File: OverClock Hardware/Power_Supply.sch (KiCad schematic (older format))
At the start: 10 parts

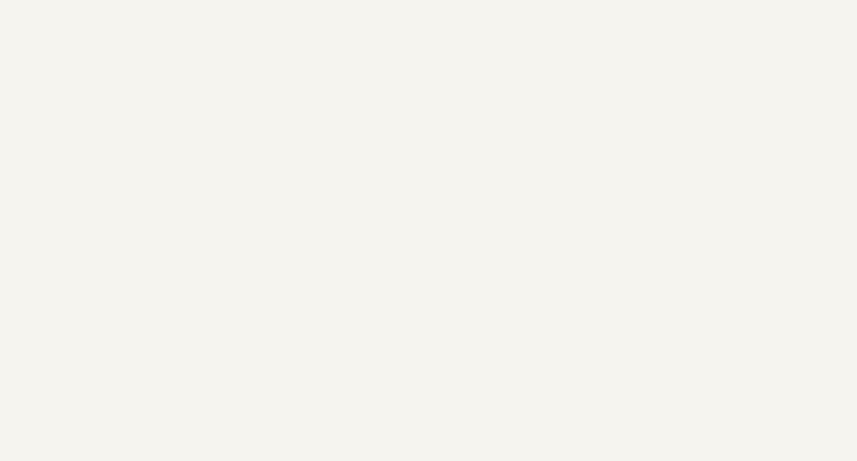
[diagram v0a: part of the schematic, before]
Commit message: Added JTAG Header
Added a JTAG header and interfaced it to the FPGA as per: page 16 https://www.intel.com/content/dam/www/programmable/us/en/pdfs/literature/hb/max-10/m10_guidelines.pdf
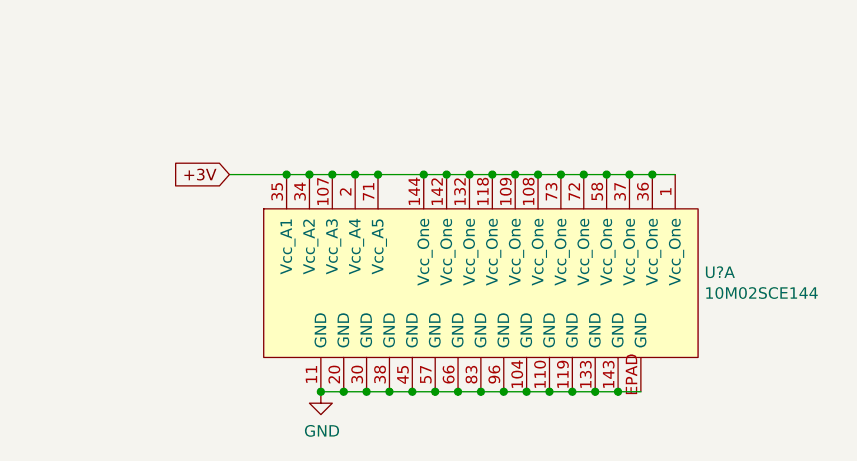
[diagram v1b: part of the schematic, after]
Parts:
- added U?: 10M02SCE144, Maxted Libs:QFP-144_EPAD_20x20_Pitch0.5mm, symbol Maxted_Libs:10M02SCE144
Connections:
- wire segments 41 -> 72
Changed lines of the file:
@@
 	7150 1400 7000 1400
 Connection ~ 7000 1400
+$Comp
+L Maxted_Libs:10M02SCE144 U?
+U 1 1 5C66E890
+P 6950 3900
+F 0 "U?" H 7928 4021 50  0000 L CNN
+F 1 "10M02SCE144" H 7928 3930 50  0000 L CNN
+F 2 "Maxted Libs:QFP-144_EPAD_20x20_Pitch0.5mm" H 7950 4700 50  0001 C CNN
+F 3 "" V 7300 4050 50  0001 C CNN
+	1    6950 3900
+	1    0    0    -1
+$EndComp
+$Comp
+L power:GND #PWR?
+U 1 1 5C66E982
+P 6250 4300
+F 0 "#PWR?" H 6250 4050 50  0001 C CNN
+F 1 "GND" H 6255 4127 50  0000 C CNN
+F 2 "" H 6250 4300 50  0001 C CNN
+F 3 "" H 6250 4300 50  0001 C CNN
+	1    6250 4300
+	1    0    0    -1
+$EndComp
+Wire Wire Line
+	7650 4300 7550 4300
+Connection ~ 6250 4300
+Connection ~ 6350 4300
+Wire Wire Line
+	6350 4300 6250 4300
+Connection ~ 6450 4300
+Wire Wire Line
+	6450 4300 6350 4300
+Connection ~ 6550 4300
+Wire Wire Line
+	6550 4300 6450 4300
+Connection ~ 6650 4300
+Wire Wire Line
+	6650 4300 6550 4300
+Connection ~ 6750 4300
+Wire Wire Line
+	6750 4300 6650 4300
+Connection ~ 6850 4300
+Wire Wire Line
+	6850 4300 6750 4300
+Connection ~ 6950 4300
+Wire Wire Line
+	6950 4300 6850 4300
+Connection ~ 7050 4300
+Wire Wire Line
+	7050 4300 6950 4300
+Connection ~ 7150 4300
+Wire Wire Line
+	7150 4300 7050 4300
+Connection ~ 7250 4300
+Wire Wire Line
+	7250 4300 7150 4300
+Connection ~ 7350 4300
+Wire Wire Line
+	7350 4300 7250 4300
+Connection ~ 7450 4300
+Wire Wire Line
+	7450 4300 7350 4300
+Connection ~ 7550 4300
+Wire Wire Line
+	7550 4300 7450 4300
+Wire Wire Line
+	7800 3350 7700 3350
+Connection ~ 6200 3350
+Wire Wire Line
+	6200 3350 6100 3350
+Connection ~ 6300 3350
+Wire Wire Line
+	6300 3350 6200 3350
+Connection ~ 6400 3350
+Wire Wire Line
+	6400 3350 6300 3350
+Connection ~ 6500 3350
+Wire Wire Line
+	6500 3350 6400 3350
+Connection ~ 6700 3350
+Wire Wire Line
+	6700 3350 6500 3350
+Connection ~ 6800 3350
+Wire Wire Line
+	6800 3350 6700 3350
+Connection ~ 6900 3350
+Wire Wire Line
+	6900 3350 6800 3350
+Connection ~ 7000 3350
+Wire Wire Line
+	7000 3350 6900 3350
+Connection ~ 7100 3350
+Wire Wire Line
+	7100 3350 7000 3350
+Connection ~ 7200 3350
+Wire Wire Line
+	7200 3350 7100 3350
+Connection ~ 7300 3350
+Wire Wire Line
+	7300 3350 7200 3350
+Connection ~ 7400 3350
+Wire Wire Line
+	7400 3350 7300 3350
+Connection ~ 7500 3350
+Wire Wire Line
+	7500 3350 7400 3350
+Connection ~ 7600 3350
+Wire Wire Line
+	7600 3350 7500 3350
+Connection ~ 7700 3350
+Wire Wire Line
+	7700 3350 7600 3350
+Text GLabel 5850 3350 0    50   Input ~ 0
++3V
+Wire Wire Line
+	5850 3350 6100 3350
+Connection ~ 6100 3350
 $EndSCHEMATC

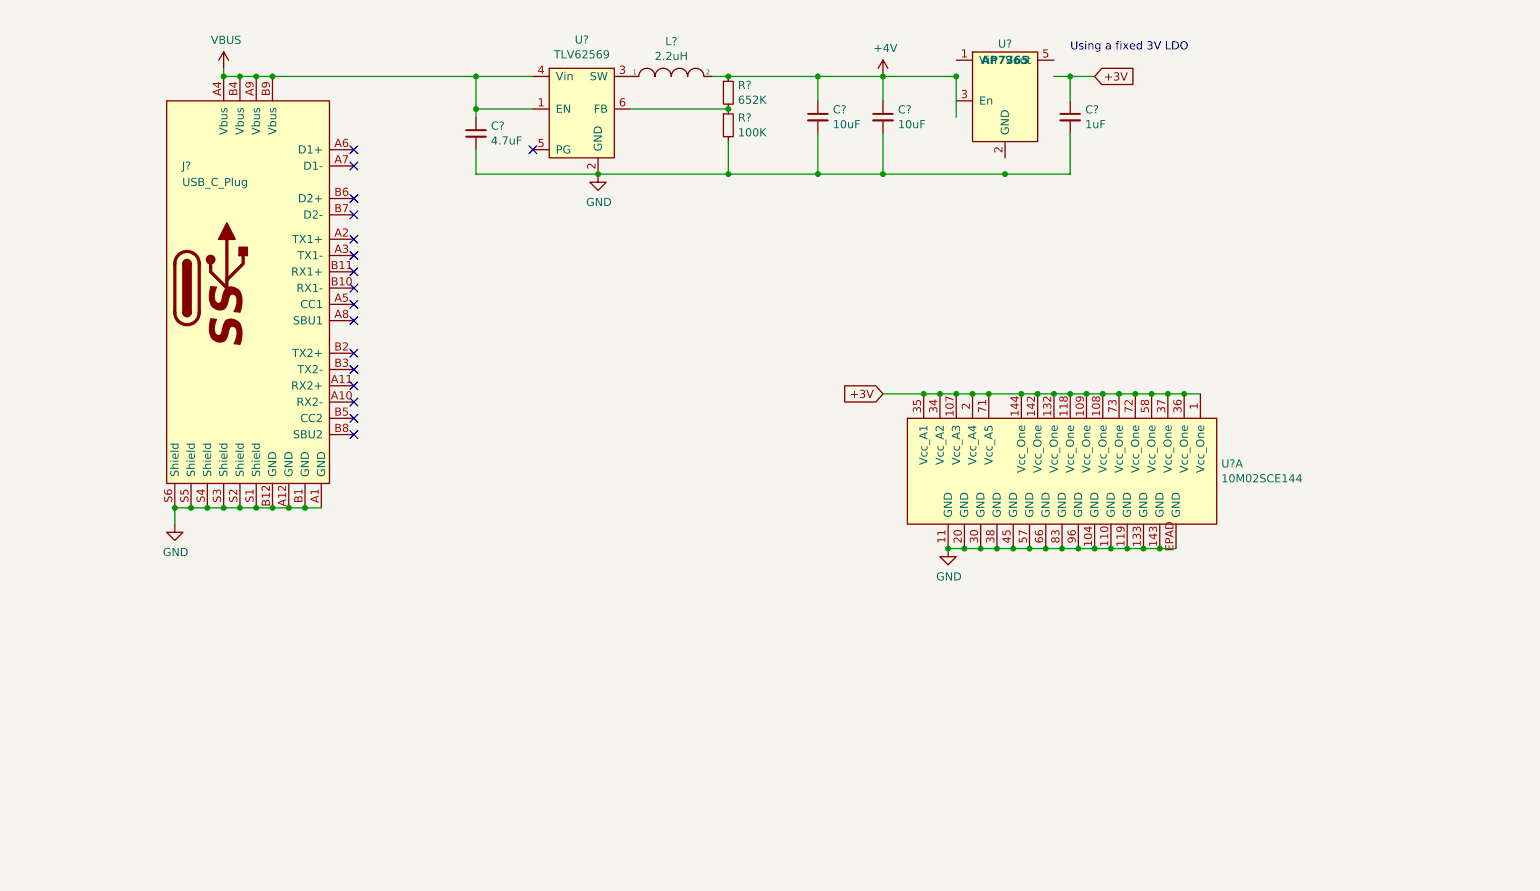
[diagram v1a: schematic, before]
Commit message: Added Decoupling strategy and started adding decoupling capacitors
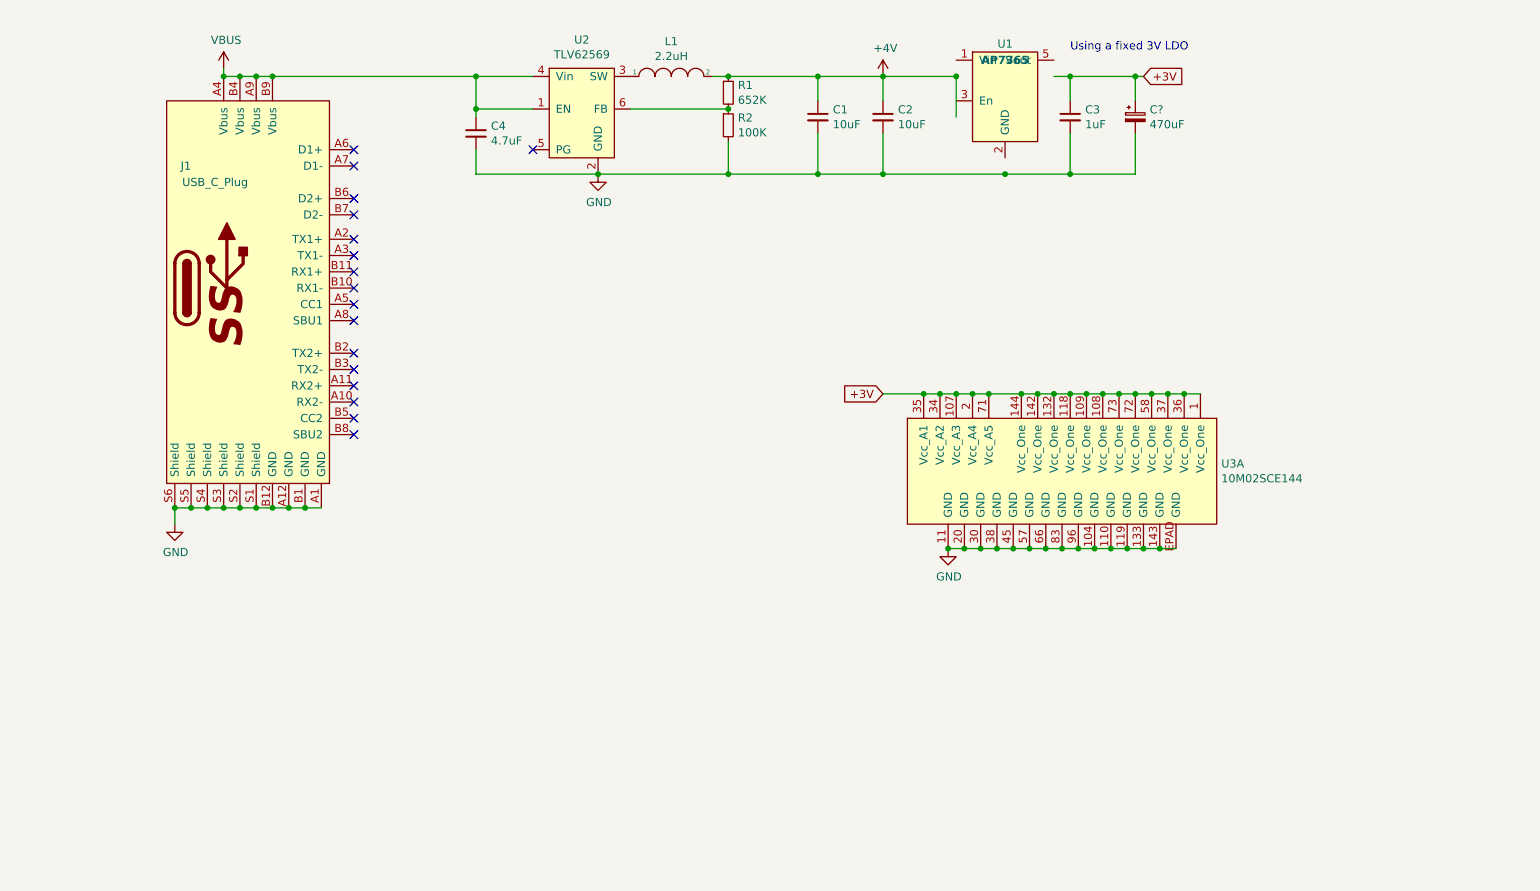
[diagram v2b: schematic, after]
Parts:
- added C?: 470uF, symbol Device:CP_Small
- gave numbers to parts that had none: 11
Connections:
- wire segments 72 -> 76
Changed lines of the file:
@@
 P 1950 2700
 AR Path="/5C666559" Ref="J?"  Part="1"
-AR Path="/5C656C49/5C666559" Ref="J?"  Part="1"
-F 0 "J?" H 1600 3450 50  0000 R CNN
+AR Path="/5C656C49/5C666559" Ref="J1"  Part="1"
+F 0 "J1" H 1600 3450 50  0000 R CNN
 F 1 "USB_C_Plug" H 1950 3350 50  0000 R CNN
 F 2 "Maxted Libs:Hirose_USB_C_Connector" H 2600 3050 50  0001 C CNN
@@
 P 1500 4150
 AR Path="/5C666560" Ref="#PWR?"  Part="1"
-AR Path="/5C656C49/5C666560" Ref="#PWR?"  Part="1"
-F 0 "#PWR?" H 1500 3900 50  0001 C CNN
+AR Path="/5C656C49/5C666560" Ref="#PWR04"  Part="1"
+F 0 "#PWR04" H 1500 3900 50  0001 C CNN
 F 1 "GND" H 1505 3977 50  0000 C CNN
 F 2 "" H 1500 4150 50  0001 C CNN
@@
 P 1800 1350
 AR Path="/5C666579" Ref="#PWR?"  Part="1"
-AR Path="/5C656C49/5C666579" Ref="#PWR?"  Part="1"
-F 0 "#PWR?" H 1800 1200 50  0001 C CNN
+AR Path="/5C656C49/5C666579" Ref="#PWR01"  Part="1"
+F 0 "#PWR01" H 1800 1200 50  0001 C CNN
 F 1 "VBUS" H 1815 1523 50  0000 C CNN
 F 2 "" H 1800 1350 50  0001 C CNN
@@
 P 3950 1650
 AR Path="/5C666597" Ref="U?"  Part="1"
-AR Path="/5C656C49/5C666597" Ref="U?"  Part="1"
-F 0 "U?" H 4000 2125 50  0000 C CNN
+AR Path="/5C656C49/5C666597" Ref="U2"  Part="1"
+F 0 "U2" H 4000 2125 50  0000 C CNN
 F 1 "TLV62569" H 4000 2034 50  0000 C CNN
 F 2 "Maxted Libs:SOT23-6" H 3600 1350 50  0001 C CNN
@@
 P 4100 2000
 AR Path="/5C6665A0" Ref="#PWR?"  Part="1"
-AR Path="/5C656C49/5C6665A0" Ref="#PWR?"  Part="1"
-F 0 "#PWR?" H 4100 1750 50  0001 C CNN
+AR Path="/5C656C49/5C6665A0" Ref="#PWR03"  Part="1"
+F 0 "#PWR03" H 4100 1750 50  0001 C CNN
 F 1 "GND" H 4105 1827 50  0000 C CNN
 F 2 "" H 4100 2000 50  0001 C CNN
@@
 P 4550 1400
 AR Path="/5C6665A7" Ref="L?"  Part="1"
-AR Path="/5C656C49/5C6665A7" Ref="L?"  Part="1"
-F 0 "L?" H 4550 1615 50  0000 C CNN
+AR Path="/5C656C49/5C6665A7" Ref="L1"  Part="1"
+F 0 "L1" H 4550 1615 50  0000 C CNN
 F 1 "2.2uH" H 4550 1524 50  0000 C CNN
 F 2 "Maxted Libs:IHLP3232" H 4550 1400 50  0001 C CNN
@@
 P 4900 1500
 AR Path="/5C6665AE" Ref="R?"  Part="1"
-AR Path="/5C656C49/5C6665AE" Ref="R?"  Part="1"
-F 0 "R?" H 4959 1546 50  0000 L CNN
+AR Path="/5C656C49/5C6665AE" Ref="R1"  Part="1"
+F 0 "R1" H 4959 1546 50  0000 L CNN
 F 1 "652K" H 4959 1455 50  0000 L CNN
 F 2 "Resistor_SMD:R_0805_2012Metric_Pad1.15x1.40mm_HandSolder" H 4900 1500 50  0001 C CNN
@@
 P 4900 1700
 AR Path="/5C6665B5" Ref="R?"  Part="1"
-AR Path="/5C656C49/5C6665B5" Ref="R?"  Part="1"
-F 0 "R?" H 4959 1746 50  0000 L CNN
+AR Path="/5C656C49/5C6665B5" Ref="R2"  Part="1"
+F 0 "R2" H 4959 1746 50  0000 L CNN
 F 1 "100K" H 4959 1655 50  0000 L CNN
 F 2 "Resistor_SMD:R_0805_2012Metric_Pad1.15x1.40mm_HandSolder" H 4900 1700 50  0001 C CNN
@@
 P 5450 1650
 AR Path="/5C6665BF" Ref="C?"  Part="1"
-AR Path="/5C656C49/5C6665BF" Ref="C?"  Part="1"
-F 0 "C?" H 5542 1696 50  0000 L CNN
+AR Path="/5C656C49/5C6665BF" Ref="C1"  Part="1"
+F 0 "C1" H 5542 1696 50  0000 L CNN
 F 1 "10uF" H 5542 1605 50  0000 L CNN
 F 2 "Capacitor_SMD:C_0805_2012Metric_Pad1.15x1.40mm_HandSolder" H 5450 1650 50  0001 C CNN
@@
 P 5850 1650
 AR Path="/5C6665C6" Ref="C?"  Part="1"
-AR Path="/5C656C49/5C6665C6" Ref="C?"  Part="1"
-F 0 "C?" H 5942 1696 50  0000 L CNN
+AR Path="/5C656C49/5C6665C6" Ref="C2"  Part="1"
+F 0 "C2" H 5942 1696 50  0000 L CNN
 F 1 "10uF" H 5942 1605 50  0000 L CNN
 F 2 "Capacitor_SMD:C_0805_2012Metric_Pad1.15x1.40mm_HandSolder" H 5850 1650 50  0001 C CNN
@@
 P 3350 1750
 AR Path="/5C6665DC" Ref="C?"  Part="1"
-AR Path="/5C656C49/5C6665DC" Ref="C?"  Part="1"
-F 0 "C?" H 3442 1796 50  0000 L CNN
+AR Path="/5C656C49/5C6665DC" Ref="C4"  Part="1"
+F 0 "C4" H 3442 1796 50  0000 L CNN
 F 1 "4.7uF" H 3442 1705 50  0000 L CNN
 F 2 "Capacitor_SMD:C_0805_2012Metric_Pad1.15x1.40mm_HandSolder" H 3350 1750 50  0001 C CNN
@@
 P 5850 1400
 AR Path="/5C6665EC" Ref="#PWR?"  Part="1"
-AR Path="/5C656C49/5C6665EC" Ref="#PWR?"  Part="1"
-F 0 "#PWR?" H 5850 1250 50  0001 C CNN
+AR Path="/5C656C49/5C6665EC" Ref="#PWR02"  Part="1"
+F 0 "#PWR02" H 5850 1250 50  0001 C CNN
 F 1 "+4V" H 5865 1573 50  0000 C CNN
 F 2 "" H 5850 1400 50  0001 C CNN
@@
 P 6600 1500
 AR Path="/5C6665F4" Ref="U?"  Part="1"
-AR Path="/5C656C49/5C6665F4" Ref="U?"  Part="1"
-F 0 "U?" H 6600 1800 50  0000 C CNN
+AR Path="/5C656C49/5C6665F4" Ref="U1"  Part="1"
+F 0 "U1" H 6600 1800 50  0000 C CNN
 F 1 "AP7365" H 6600 1700 50  0000 C CNB
 F 2 "Maxted Libs:SOT-23-5" H 6600 950 50  0001 C CNN
@@
 	5850 2000 6600 2000
 Connection ~ 5850 2000
-Text GLabel 7150 1400 2    50   Input ~ 0
+Text GLabel 7450 1400 2    50   Input ~ 0
 +3V
 $Comp
@@
 P 7000 1650
 AR Path="/5C666601" Ref="C?"  Part="1"
-AR Path="/5C656C49/5C666601" Ref="C?"  Part="1"
-F 0 "C?" H 7092 1696 50  0000 L CNN
+AR Path="/5C656C49/5C666601" Ref="C3"  Part="1"
+F 0 "C3" H 7092 1696 50  0000 L CNN
 F 1 "1uF" H 7092 1605 50  0000 L CNN
 F 2 "Capacitor_SMD:C_0805_2012Metric_Pad1.15x1.40mm_HandSolder" H 7000 1650 50  0001 C CNN
@@
 Wire Wire Line
 	7000 1750 7000 2000
-Wire Wire Line
-	7150 1400 7000 1400
 Connection ~ 7000 1400
 $Comp
-L Maxted_Libs:10M02SCE144 U?
+L Maxted_Libs:10M02SCE144 U3
 U 1 1 5C66E890
 P 6950 3900
-F 0 "U?" H 7928 4021 50  0000 L CNN
+F 0 "U3" H 7928 4021 50  0000 L CNN
 F 1 "10M02SCE144" H 7928 3930 50  0000 L CNN
 F 2 "Maxted Libs:QFP-144_EPAD_20x20_Pitch0.5mm" H 7950 4700 50  0001 C CNN
@@
 $EndComp
 $Comp
-L power:GND #PWR?
+L power:GND #PWR05
 U 1 1 5C66E982
 P 6250 4300
-F 0 "#PWR?" H 6250 4050 50  0001 C CNN
+F 0 "#PWR05" H 6250 4050 50  0001 C CNN
 F 1 "GND" H 6255 4127 50  0000 C CNN
 F 2 "" H 6250 4300 50  0001 C CNN
@@
 	5850 3350 6100 3350
 Connection ~ 6100 3350
+Wire Wire Line
+	7000 1400 7400 1400
+Wire Wire Line
+	7400 1550 7400 1400
+Connection ~ 7400 1400
+Wire Wire Line
+	7400 1400 7450 1400
+Wire Wire Line
+	7400 1750 7400 2000
+Wire Wire Line
+	7400 2000 7000 2000
+Connection ~ 7000 2000
+$Comp
+L Device:CP_Small C?
+U 1 1 5C6DC80E
+P 7400 1650
+F 0 "C?" H 7488 1696 50  0000 L CNN
+F 1 "470uF" H 7488 1605 50  0000 L CNN
+F 2 "" H 7400 1650 50  0001 C CNN
+F 3 "~" H 7400 1650 50  0001 C CNN
+	1    7400 1650
+	1    0    0    -1
+$EndComp
 $EndSCHEMATC

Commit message: Added Decoupling Caps for FPGA core
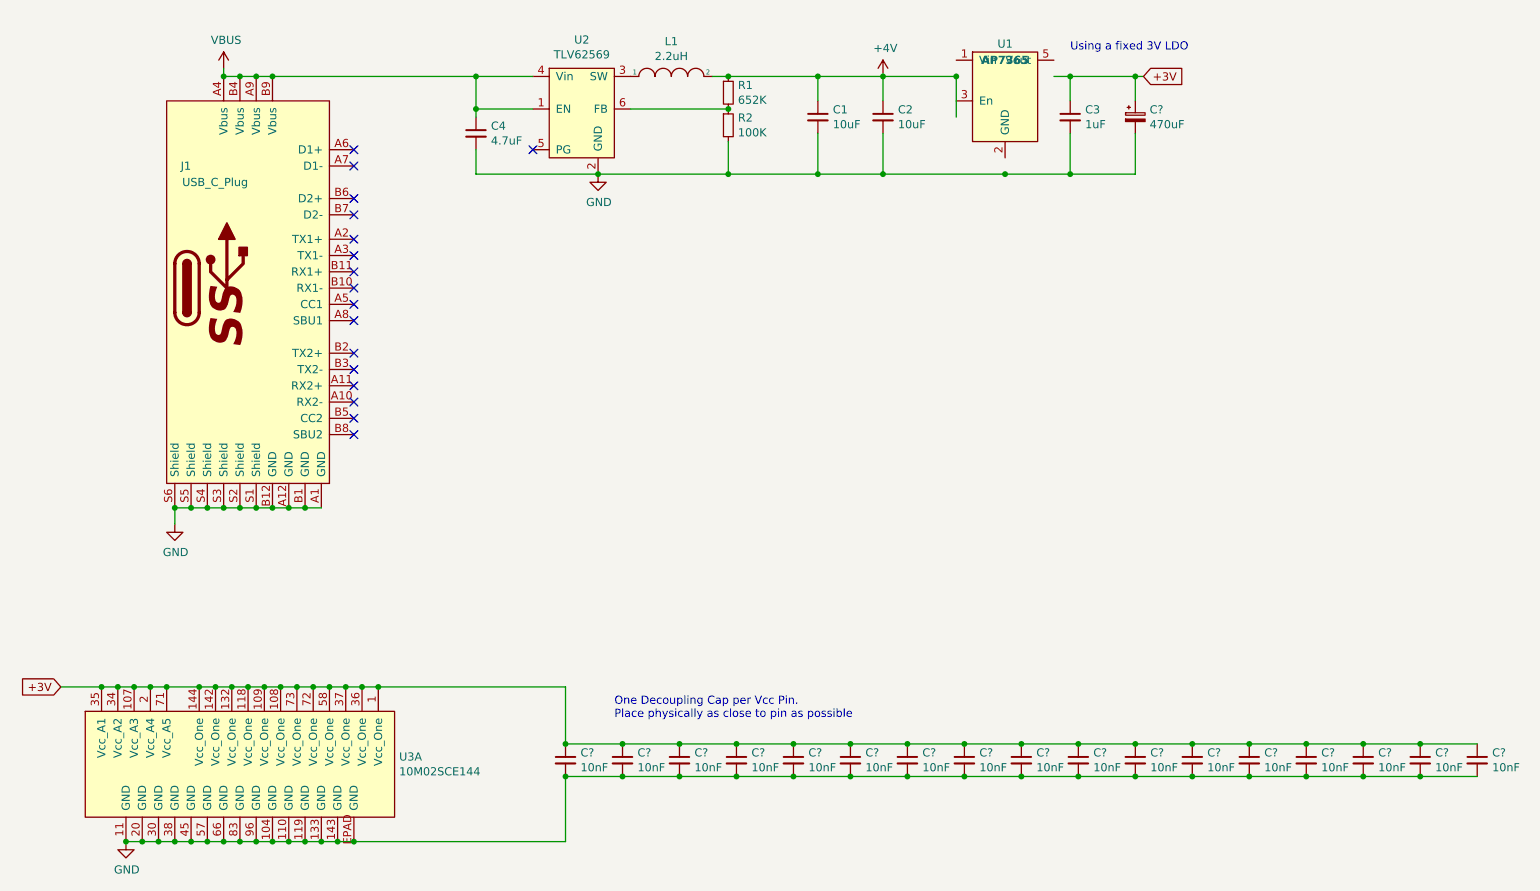
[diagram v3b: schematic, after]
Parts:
- added C? (x17): 10nF, Capacitor_SMD:C_0603_1608Metric_Pad1.05x0.95mm_HandSolder, symbol Device:C_Small
- C?: footprint (none) -> Maxted Libs:293D
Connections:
- wire segments 76 -> 112
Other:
- note added: "One Decoupling Cap per Vcc Pin.\nPlace physically as close to pin as possible"
- moved on the sheet: U3A
